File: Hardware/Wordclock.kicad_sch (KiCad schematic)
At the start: 42 parts, among them J101 USB_C_Receptacle, J102 PROGRAMMING, J103 LED_STRIP, Q101 Q_NPN_BEC, Q102 Q_NPN_BEC, Q103 PhotoTransistor, SW101 HOUR, SW102 MIN, SW103 AM/PM, U101 CH340C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

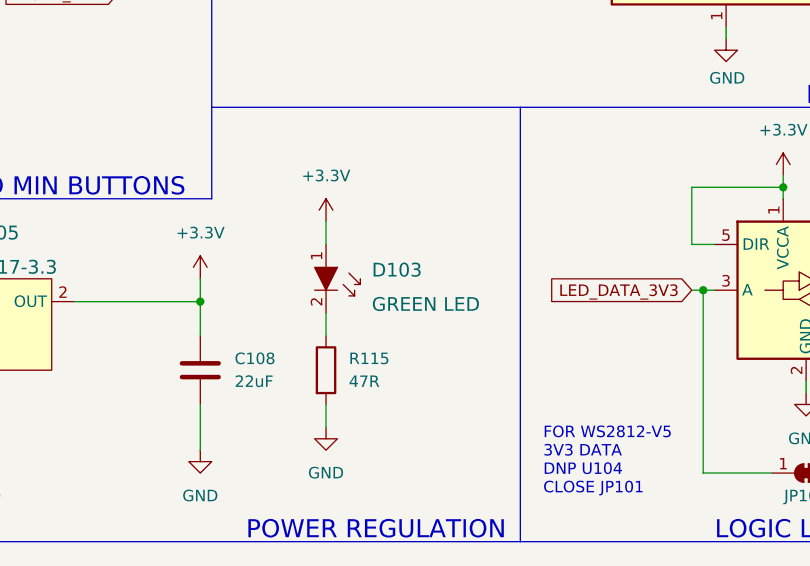
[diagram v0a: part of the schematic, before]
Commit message: Corrected D103 LED Rotation.
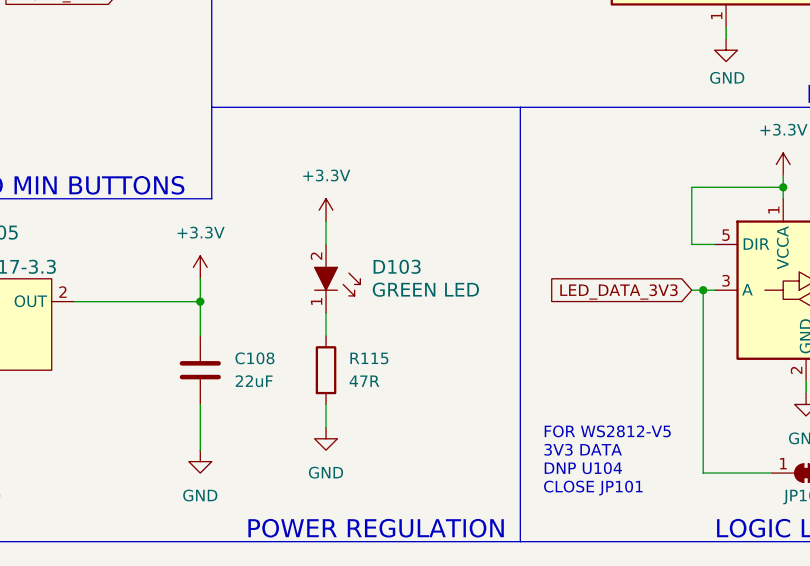
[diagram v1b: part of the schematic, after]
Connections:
- net +3V3: now also D103.2; no longer D103.1
- net at R115.1: now also D103.1; no longer D103.2
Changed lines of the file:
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@@
   (symbol (lib_id "dk_LED-Indication-Discrete:LG_R971-KN-1") (at 93.98 168.91 270) (unit 1)
     (in_bom yes) (on_board yes)
-    (property "Reference" "D103" (id 0) (at 99.06 166.6875 90)
+    (property "Reference" "D103" (id 0) (at 99.06 166.37 90)
       (effects (font (size 1.524 1.524)) (justify left))
     )
-    (property "Value" "GREEN LED" (id 1) (at 99.06 170.4975 90)
+    (property "Value" "GREEN LED" (id 1) (at 99.06 168.91 90)
       (effects (font (size 1.524 1.524)) (justify left))
     )
-    (property "Footprint" "LED_SMD:LED_0805_2012Metric" (id 2) (at 99.06 173.99 0)
+    (property "Footprint" "LED_SMD:LED_0805_2012Metric" (id 2) (at 88.9 173.99 0)
       (effects (font (size 1.524 1.524)) (justify left) hide)
     )
-    (property "Datasheet" "https://dammedia.osram.info/media/resource/hires/osram-dam-2493936/LG%20R971.pdf" (id 3) (at 101.6 173.99 0)
+    (property "Datasheet" "https://dammedia.osram.info/media/resource/hires/osram-dam-2493936/LG%20R971.pdf" (id 3) (at 88.9 176.53 0)
       (effects (font (size 1.524 1.524)) (justify left) hide)
     )
-    (property "Digi-Key_PN" "475-1410-1-ND" (id 4) (at 104.14 173.99 0)
+    (property "Digi-Key_PN" "475-1410-1-ND" (id 4) (at 88.9 179.07 0)
       (effects (font (size 1.524 1.524)) (justify left) hide)
     )
-    (property "MPN" "LG R971-KN-1" (id 5) (at 106.68 173.99 0)
+    (property "MPN" "LG R971-KN-1" (id 5) (at 88.9 181.61 0)
       (effects (font (size 1.524 1.524)) (justify left) hide)
     )
-    (property "Category" "Optoelectronics" (id 6) (at 109.22 173.99 0)
+    (property "Category" "Optoelectronics" (id 6) (at 88.9 184.15 0)
       (effects (font (size 1.524 1.524)) (justify left) hide)
     )
-    (property "Family" "LED Indication - Discrete" (id 7) (at 111.76 173.99 0)
+    (property "Family" "LED Indication - Discrete" (id 7) (at 88.9 186.69 0)
       (effects (font (size 1.524 1.524)) (justify left) hide)
     )
-    (property "DK_Datasheet_Link" "https://dammedia.osram.info/media/resource/hires/osram-dam-2493936/LG%20R971.pdf" (id 8) (at 114.3 173.99 0)
+    (property "DK_Datasheet_Link" "https://dammedia.osram.info/media/resource/hires/osram-dam-2493936/LG%20R971.pdf" (id 8) (at 88.9 189.23 0)
       (effects (font (size 1.524 1.524)) (justify left) hide)
     )
-    (property "DK_Detail_Page" "/product-detail/en/osram-opto-semiconductors-inc/LG-R971-KN-1/475-1410-1-ND/1802598" (id 9) (at 116.84 173.99 0)
+    (property "DK_Detail_Page" "/product-detail/en/osram-opto-semiconductors-inc/LG-R971-KN-1/475-1410-1-ND/1802598" (id 9) (at 88.9 191.77 0)
       (effects (font (size 1.524 1.524)) (justify left) hide)
     )
-    (property "Description" "LED GREEN DIFFUSED 0805 SMD" (id 10) (at 119.38 173.99 0)
+    (property "Description" "LED GREEN DIFFUSED 0805 SMD" (id 10) (at 88.9 194.31 0)
       (effects (font (size 1.524 1.524)) (justify left) hide)
     )
-    (property "Manufacturer" "OSRAM Opto Semiconductors Inc." (id 11) (at 121.92 173.99 0)
+    (property "Manufacturer" "OSRAM Opto Semiconductors Inc." (id 11) (at 88.9 196.85 0)
       (effects (font (size 1.524 1.524)) (justify left) hide)
     )
-    (property "Status" "Active" (id 12) (at 124.46 173.99 0)
+    (property "Status" "Active" (id 12) (at 88.9 199.39 0)
       (effects (font (size 1.524 1.524)) (justify left) hide)
     )
-    (property "Notes" "POWER" (id 13) (at 102.87 172.72 90)
+    (property "Notes" "POWER" (id 13) (at 90.17 177.8 90)
       (effects (font (size 1.27 1.27)) hide)
     )
+    (pin "2")
     (pin "1")
-    (pin "2")
   )
   (symbol (lib_id "Connector:Conn_01x07_Male") (at 254 105.41 0) (unit 1)
